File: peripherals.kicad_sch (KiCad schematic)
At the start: 6 parts, among them J1 WE_68715014522, J2 WE_68715014522

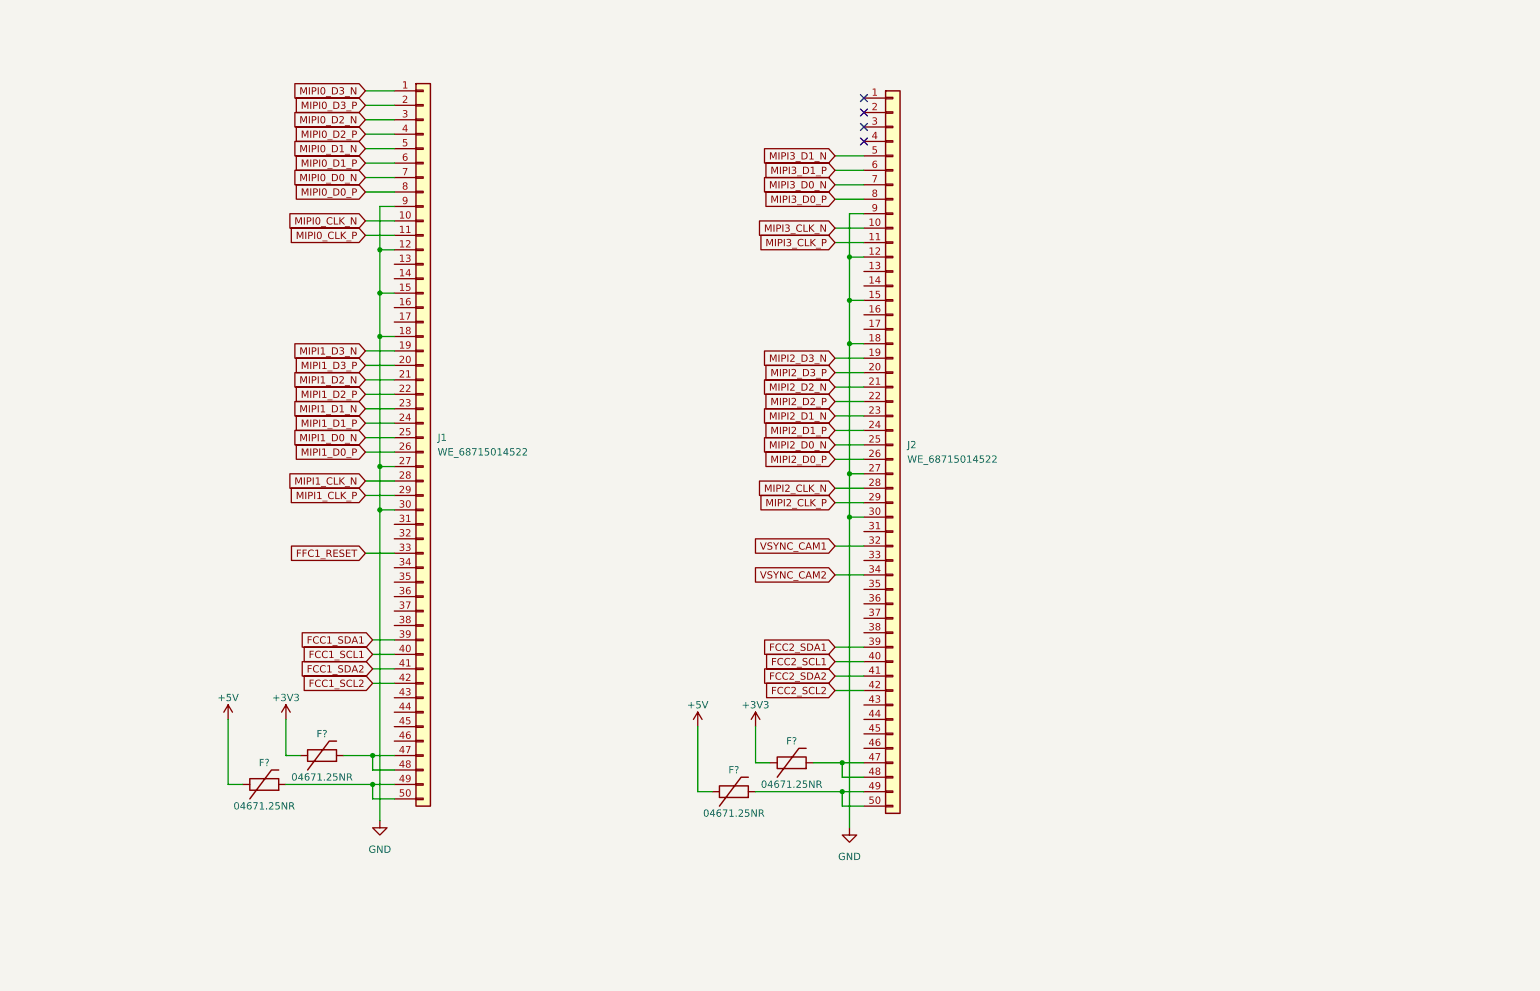
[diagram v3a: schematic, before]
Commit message: Connected Semtech to the power supply, cable driver and the FPGA
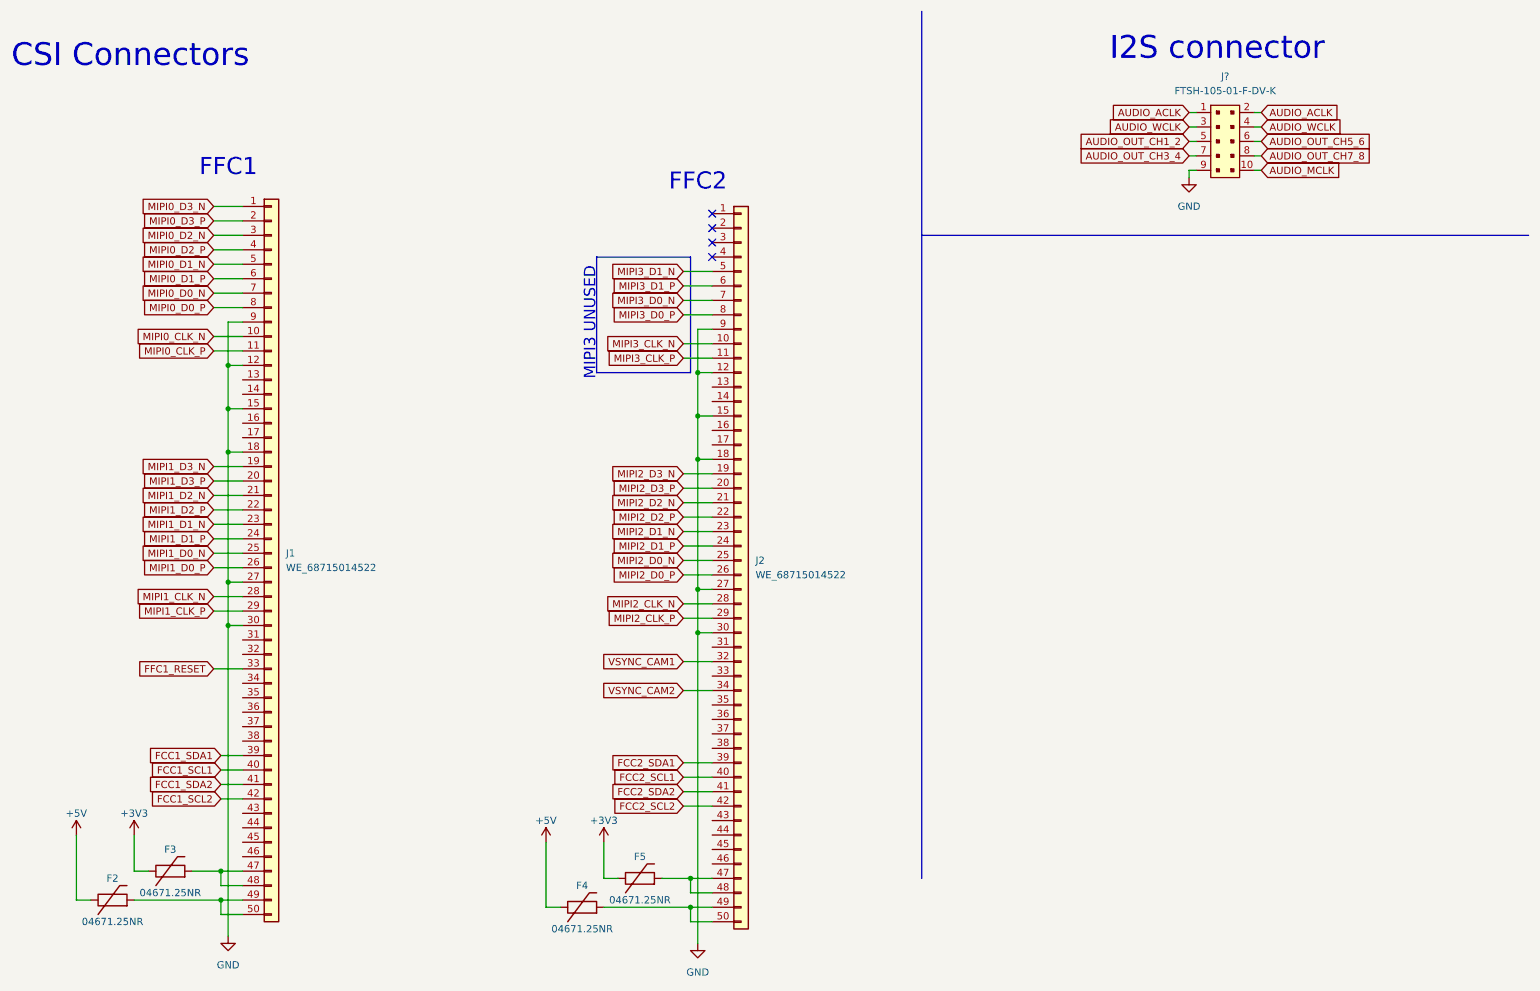
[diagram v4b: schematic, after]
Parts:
- added J?: FTSH-105-01-F-DV-K, antmicro-footprints:PinHeader_2x5_P1.27_SMD, symbol antmicroRectangularConnectorsHeadersMalePins:FTSH-105-01-F-DV-K
- gave numbers to parts that had none: 4
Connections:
- net GND: now also J?.9
- new net AUDIO_ACLK: J?.1, J?.2
- new net AUDIO_MCLK: J?.10
- new net AUDIO_OUT_CH1_2: J?.5
- new net AUDIO_OUT_CH3_4: J?.7
- new net AUDIO_OUT_CH5_6: J?.6
- new net AUDIO_OUT_CH7_8: J?.8
- new net AUDIO_WCLK: J?.3, J?.4
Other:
- note added: "CSI Connectors"
- note added: "FFC1"
- note added: "FFC2"
- note added: "I2S connector"
- note added: "MIPI3 UNUSED"
- moved on the sheet: F2, F3, F4, F5, J1, J2

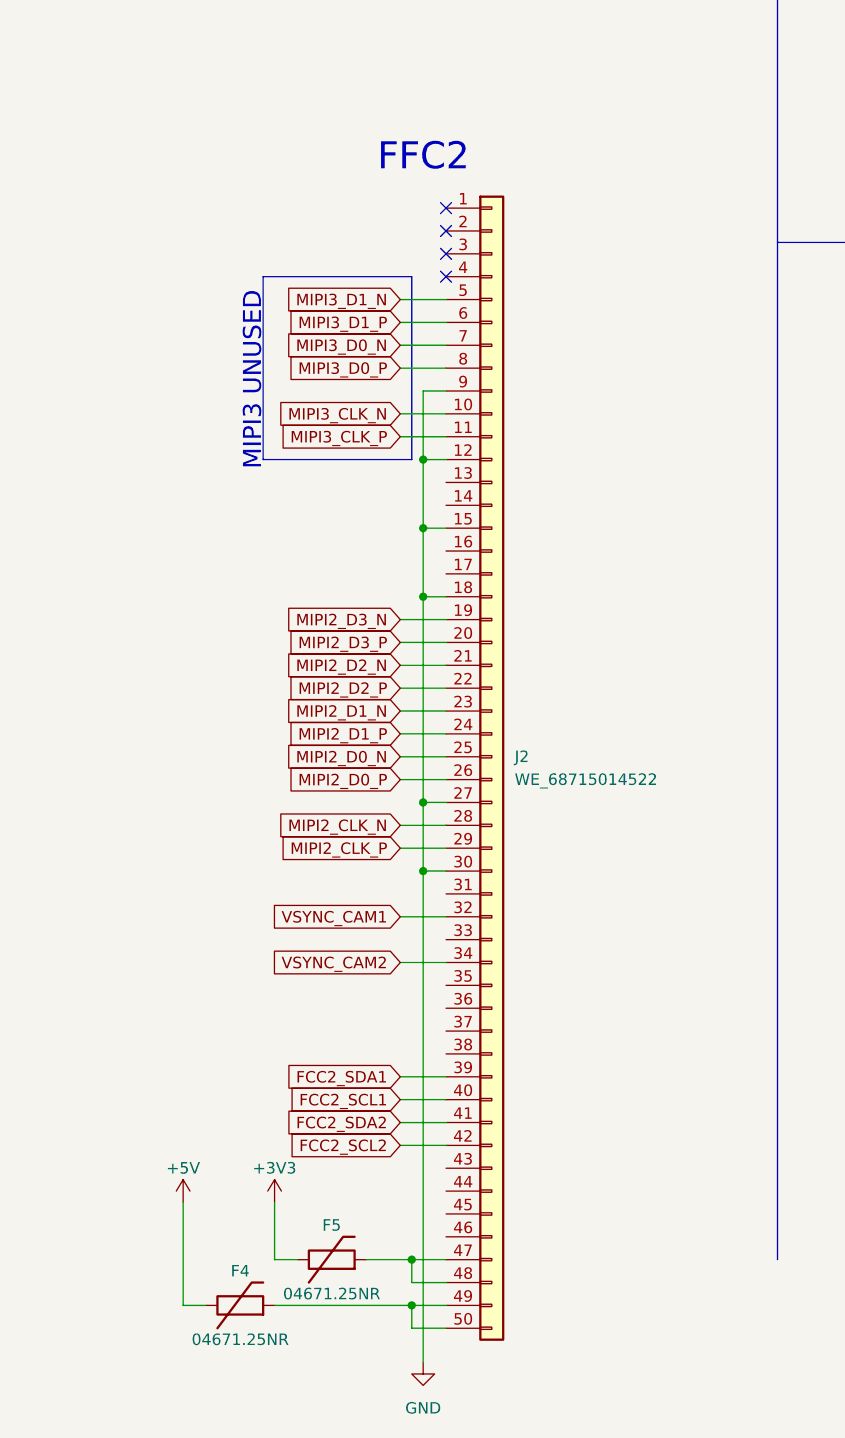
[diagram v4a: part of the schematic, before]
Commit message: Added FPGA configuration circuitry
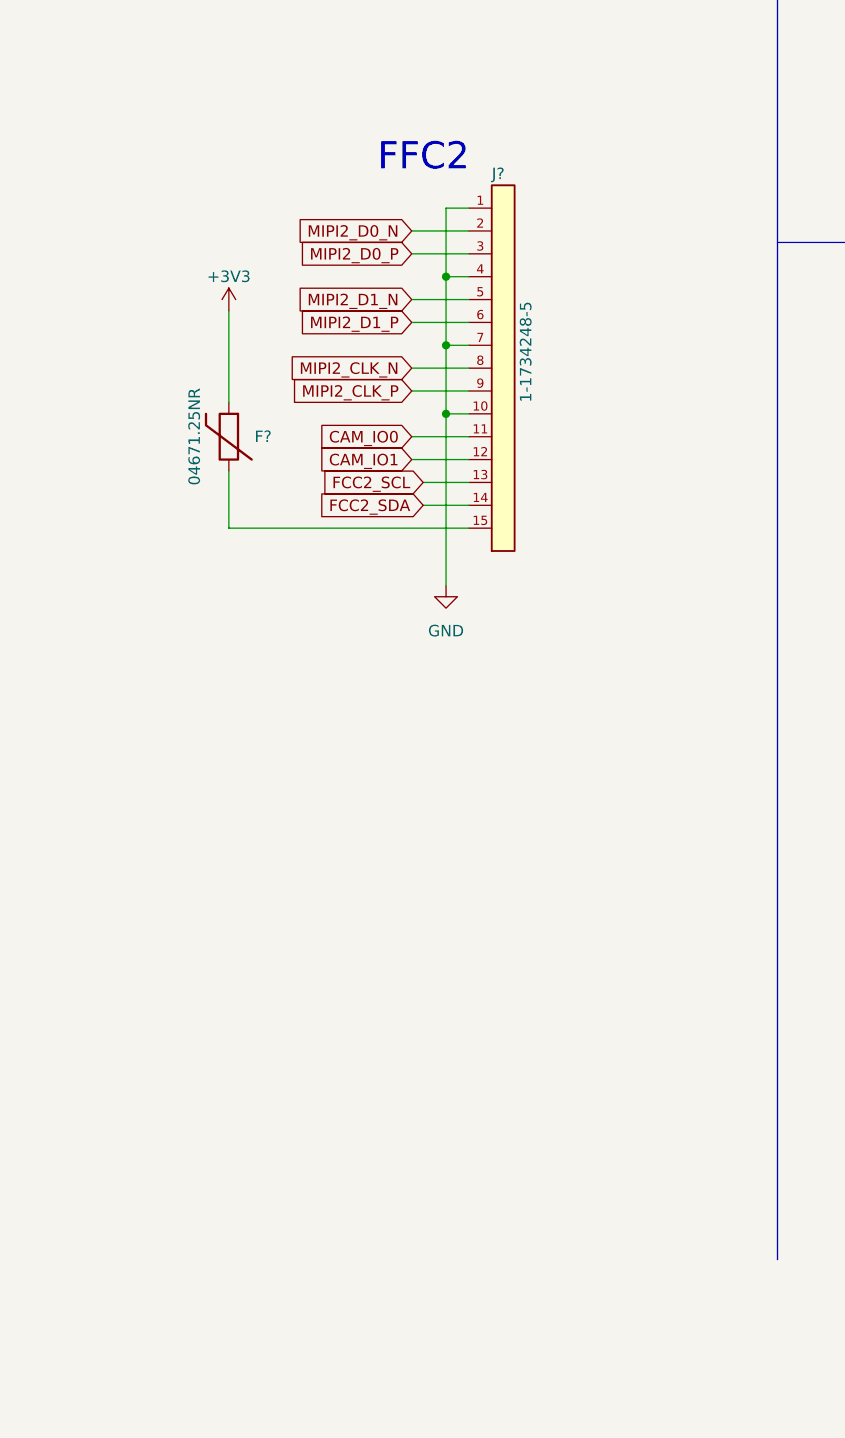
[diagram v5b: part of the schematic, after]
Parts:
- removed F4, F5: 04671.25NR, antmicro-footprints:0603-Fuse-Littelfuse-0467, symbol antmicroFuses:04671.25NR
- removed J2: WE_68715014522, antmicro-footprints:WE_68715014522, symbol antmicroFCCConnectors:WE_68715014522
- added F?: 04671.25NR, antmicro-footprints:0603-Fuse-Littelfuse-0467, symbol antmicroFuses:04671.25NR
- added J?: 1-1734248-5, antmicro-footprints:TE_1-1734248-5, symbol antmicroFCCConnectors:1-1734248-5
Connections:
- net +3V3: now also F?.2
- net GND: now also J?.1, J?.10, J?.4, J?.7
- net MIPI2_CLK_N: now also J?.8
- net MIPI2_CLK_P: now also J?.9
- net MIPI2_D0_N: now also J?.2
- net MIPI2_D0_P: now also J?.3
- net MIPI2_D1_N: now also J?.5
- net MIPI2_D1_P: now also J?.6
- new net: F?.1, J?.15
- new net CAM_IO0: J?.11
- new net CAM_IO1: J?.12
- new net FCC2_SCL: J?.13
- new net FCC2_SDA: J?.14
- no-connect marks 4 -> 0
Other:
- note removed: "MIPI3 UNUSED"
